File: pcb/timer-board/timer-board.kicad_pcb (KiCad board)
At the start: 2 copper layers, 0 parts

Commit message: Connect OLED display, position main components
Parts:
- added C1: C-100n-0402, DW-footprints:C_0402_1005Metric, B.Cu at (104.8, 123.9)
- added C10: C-2u2-0402, DW-footprints:C_0402_1005Metric, B.Cu at (134.1, 132.8)
- added C11: C-100n-0402, DW-footprints:C_0402_1005Metric, B.Cu at (132.3, 126.1)
- added C12: C-100n-0402, DW-footprints:C_0402_1005Metric, B.Cu at (128.3, 131.3)
- added C13: C-100n-0402, DW-footprints:C_0402_1005Metric, B.Cu at (120.1, 130.6)
- added C14: C-100n-0402, DW-footprints:C_0402_1005Metric, B.Cu at (117.8, 120.3)
- added C15: C-4u7-0402, DW-footprints:C_0402_1005Metric, B.Cu at (133.1, 132.8)
- added C16: C-4u7-0402, DW-footprints:C_0402_1005Metric, B.Cu at (124.8, 132.6)
- added C2: C-4u7-0402, DW-footprints:C_0402_1005Metric, B.Cu at (115.2, 121.9)
- added C3: C-4u7-0402, DW-footprints:C_0402_1005Metric, B.Cu at (111.2, 122.0)
- added C6: C-1u-0402, DW-footprints:C_0402_1005Metric, B.Cu at (117.6, 133.2)
- added C7: C-4u7-0402, DW-footprints:C_0402_1005Metric, B.Cu at (121.8, 131.3)
- added C8: C-1u-0402, DW-footprints:C_0402_1005Metric, B.Cu at (115.6, 133.2)
- added C9: C-100n-0402, DW-footprints:C_0402_1005Metric, B.Cu at (132.8, 119.7)
- added D1: PESD5Z5, DW-footprints:D_SOD-523, B.Cu at (110.0, 134.3)
- added D2: TPD2E2U06DCKR, DW-footprints:SOT-323, B.Cu at (110.7, 131.2)
- added DISP1: N096-2864KSWEG01-H30, DW-footprints:N096-2864KSWEG01-H30, B.Cu at (125.3, 135.2)
- added J1: USB-C_USB-310F-B-SU, DW-footprints:USB-C-Receptacle_USB-310-B-SU, B.Cu at (103.7, 130.0)
- added J11: Programming connector, DW-footprints:Custom-programming-connector-1x6_P1.27mm, B.Cu at (167.4, 125.3)
- added M1: DM-OLED096-636, DW-footprints:DM-OLED096-636, F.Cu at (121.2, 117.5)
- added R1: R-330r-0402, DW-footprints:R_0402_1005Metric, B.Cu at (105.8, 123.9)
- added R2: R-5k1-0402, DW-footprints:R_0402_1005Metric, B.Cu at (110.0, 126.0)
- added R3: R-5k1-0402, DW-footprints:R_0402_1005Metric, B.Cu at (111.1, 126.0)
- added R5: R-5k1-0402, DW-footprints:R_0402_1005Metric, B.Cu at (123.8, 132.6)
- added R6: R-390k-0402, DW-footprints:R_0402_1005Metric, B.Cu at (132.0, 132.8)
- added REF**: NPTH_3.2mm, DW-footprints:NPTH_3.2mm, F.Cu at (103.5, 146.5)
- added REF**: NPTH_3.2mm, DW-footprints:NPTH_3.2mm, F.Cu at (146.5, 113.5)
- added REF**: NPTH_3.2mm, DW-footprints:NPTH_3.2mm, F.Cu at (103.5, 113.5)
- added REF**: NPTH_3.2mm, DW-footprints:NPTH_3.2mm, F.Cu at (146.5, 146.5)
- added SW1: SW_KMR211NGLFS, DW-footprints:SW_KMR211NGLFS, B.Cu at (137.0, 107.0)
- added SW2: SW_KMR211NGLFS, DW-footprints:SW_KMR211NGLFS, F.Cu at (115.0, 144.3)
- added SW3: SW_KMR211NGLFS, DW-footprints:SW_KMR211NGLFS, F.Cu at (135.0, 144.3)
- added SW4: SW_KMR211NGLFS, DW-footprints:SW_KMR211NGLFS, F.Cu at (125.0, 144.3)
- added U1: STM32F411RET6, DW-footprints:LQFP-64_10x10mm_P0.5mm, B.Cu at (125.0, 124.0)
- added U2: TSSP58038, OptoDevice:Vishay_MINICAST-3Pin, B.Cu at (122.5, 113.8)
- added U3: AMS1117-3.3, Package_TO_SOT_SMD:SOT-223-3_TabPin2, B.Cu at (112.5, 116.8)
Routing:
- net GND: track 0.00 -> 17.5 mm, vias 0 -> 11
- net +3V3: track 0.00 -> 15.1 mm, vias 0 -> 6
- net /MCU/OSC_IN: track 0.00 -> 5.39 mm
- net /MCU/OSC_OUT: track 0.00 -> 3.73 mm
- net /Display/C1N: track 0.00 -> 2.09 mm
- net /Display/C2P: track 0.00 -> 2.09 mm
- net /Display/VCC: track 0.00 -> 2.00 mm
- net /Display/IREF: track 0.00 -> 2.00 mm
- net /Display/C1P: track 0.00 -> 2.00 mm
- net /Display/C2N: track 0.00 -> 1.97 mm
- net /Display/VCOMH: track 0.00 -> 1.85 mm
- net Net-(U1-VCAP1): track 0.00 -> 1.50 mm
- net /MCU/USB.D+: track 0.00 -> 0.95 mm
- net /MCU/USB.D-: track 0.00 -> 0.82 mm
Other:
- board outline added: 50 x 40 mm

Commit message: Layout power planes and different signals
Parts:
- removed M1: DM-OLED096-636, DW-footprints:DM-OLED096-636
- added C4: C-100n-0402, DW-footprints:C_0402_1005Metric, B.Cu at (128.8, 116.8)
- added TP1: TP_SMD_1mm, DW-footprints:TP_SMD_1mm, F.Cu at (140.6, 133.4)
- added TP2: TP_SMD_1mm, DW-footprints:TP_SMD_1mm, F.Cu at (142.9, 133.4)
- added kibuzzard-68E6B0E6: G***, kibuzzard-68E6B0E6, B.Cu at (116.2, 118.4)
- added kibuzzard-68E6B138: G***, kibuzzard-68E6B138, B.Cu at (115.5, 117.1)
- added kibuzzard-68E6B152: G***, kibuzzard-68E6B152, B.Cu at (115.5, 115.8)
- added kibuzzard-68E6B17C: G***, kibuzzard-68E6B17C, B.Cu at (116.2, 114.6)
- added kibuzzard-68E6B182: G***, kibuzzard-68E6B182, B.Cu at (116.2, 113.3)
- added kibuzzard-68FD2D82: G***, kibuzzard-68FD2D82, B.Cu at (116.5, 112.0)
- moved J11 50.1 mm to (117.8, 118.4)
- moved U3 23.0 mm to (108.5, 139.4), turned to 0 degrees
- moved C2 19.7 mm to (103.4, 137.6), turned to 90 degrees
- moved C3 19.6 mm to (103.4, 139.9), turned to 90 degrees
- moved SW1 8.70 mm to (134.2, 115.2), turned to -90 degrees
- moved R3 7.33 mm to (110.2, 133.3), turned to 90 degrees
- moved R2 1.83 mm to (109.0, 127.5)
- moved C1 1.58 mm to (106.4, 123.8)
- moved R1 1.58 mm to (107.4, 123.8)
- moved D1 1.41 mm to (109.0, 133.3)
- moved D2 1.10 mm to (109.9, 130.5)
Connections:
- J11 pad 4: /MCU/~{RST} -> /MCU/NRST
- J11 pad 6: /MCU/BOOT0 -> unconnected-(J11-Pad6)
- SW2 pad 3: unconnected-(SW2-Pad3) -> GND
- SW2 pad 4: unconnected-(SW2-Pad4) -> GND
- SW3 pad 3: unconnected-(SW3-Pad3) -> GND
- SW3 pad 4: unconnected-(SW3-Pad4) -> GND
- SW4 pad 3: unconnected-(SW4-Pad3) -> GND
- SW4 pad 4: unconnected-(SW4-Pad4) -> GND
- U1 pad 40: unconnected-(U1-PC9-Pad40) -> /Display/I2C.SDA
- U1 pad 41: unconnected-(U1-PA8-Pad41) -> /Display/I2C.SCL
- U2 pad 1: unconnected-(U2-OUT-Pad1) -> /IR receiver/GATE_TRIGGER
- U2 pad 2: unconnected-(U2-GND-Pad2) -> GND
- U2 pad 3: unconnected-(U2-Vs-Pad3) -> +3V3
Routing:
- net GND: track 17.5 -> 50.4 mm, vias 11 -> 41
- net /Display/I2C.SCL: track 0.00 -> 25.7 mm
- net /Display/I2C.SDA: track 0.00 -> 20.5 mm
- net /MCU/NRST: track 0.00 -> 20.5 mm
- net /MCU/USB.D-: track 0.82 -> 18.5 mm
- net /MCU/USB.D+: track 0.95 -> 17.3 mm
- net /MCU/BOOT0: track 0.00 -> 14.1 mm
- net /MCU/SWDIO: track 0.00 -> 6.90 mm
- net /MCU/SWCLK: track 0.00 -> 4.91 mm
- net /Power/VBUS: track 0.00 -> 3.65 mm
- net Net-(J1-CC1): track 0.00 -> 3.46 mm
- net Net-(J1-SHIELD): track 0.00 -> 3.19 mm
- net Net-(J1-CC2): track 0.00 -> 1.75 mm
- added copper zone on B.Cu, net +3V3
- added copper zone on F.Cu, net GND

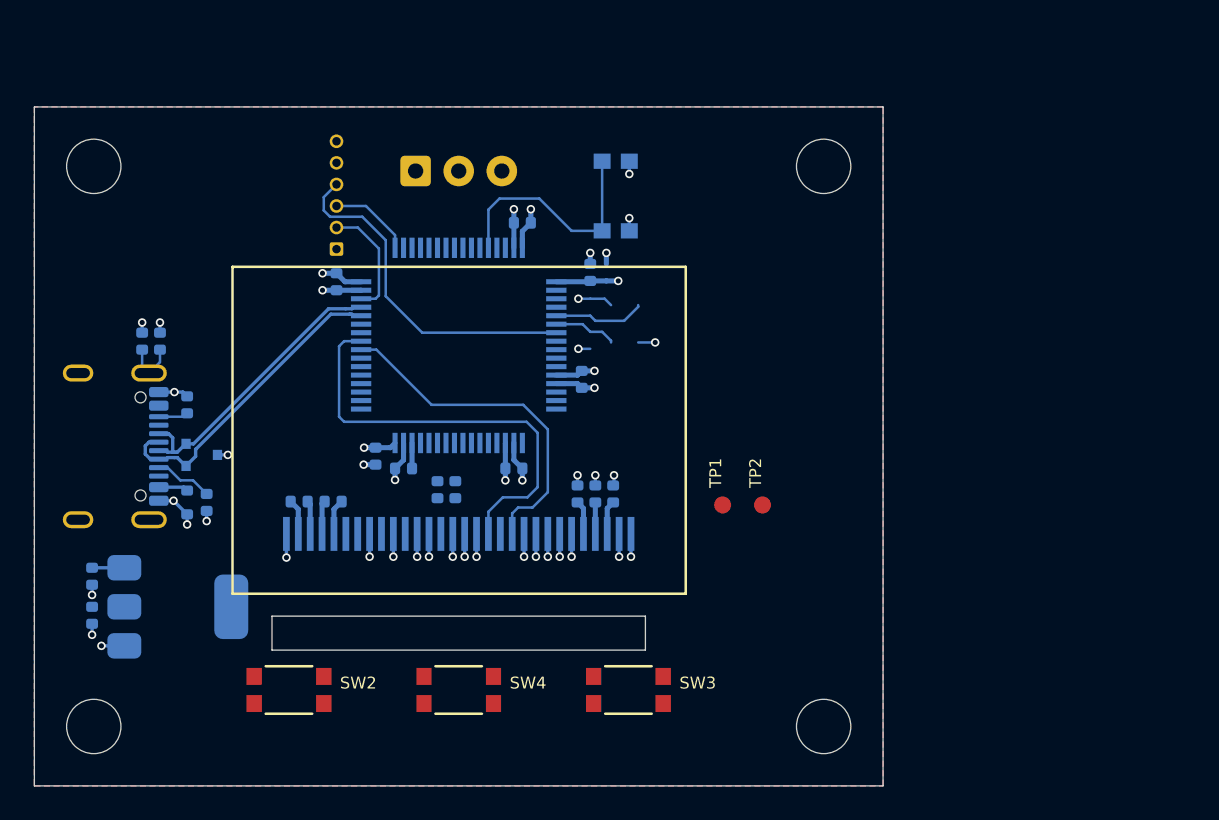
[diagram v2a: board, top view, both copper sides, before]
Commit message: Finish uncompleted schematic sections, layout most of the PCB
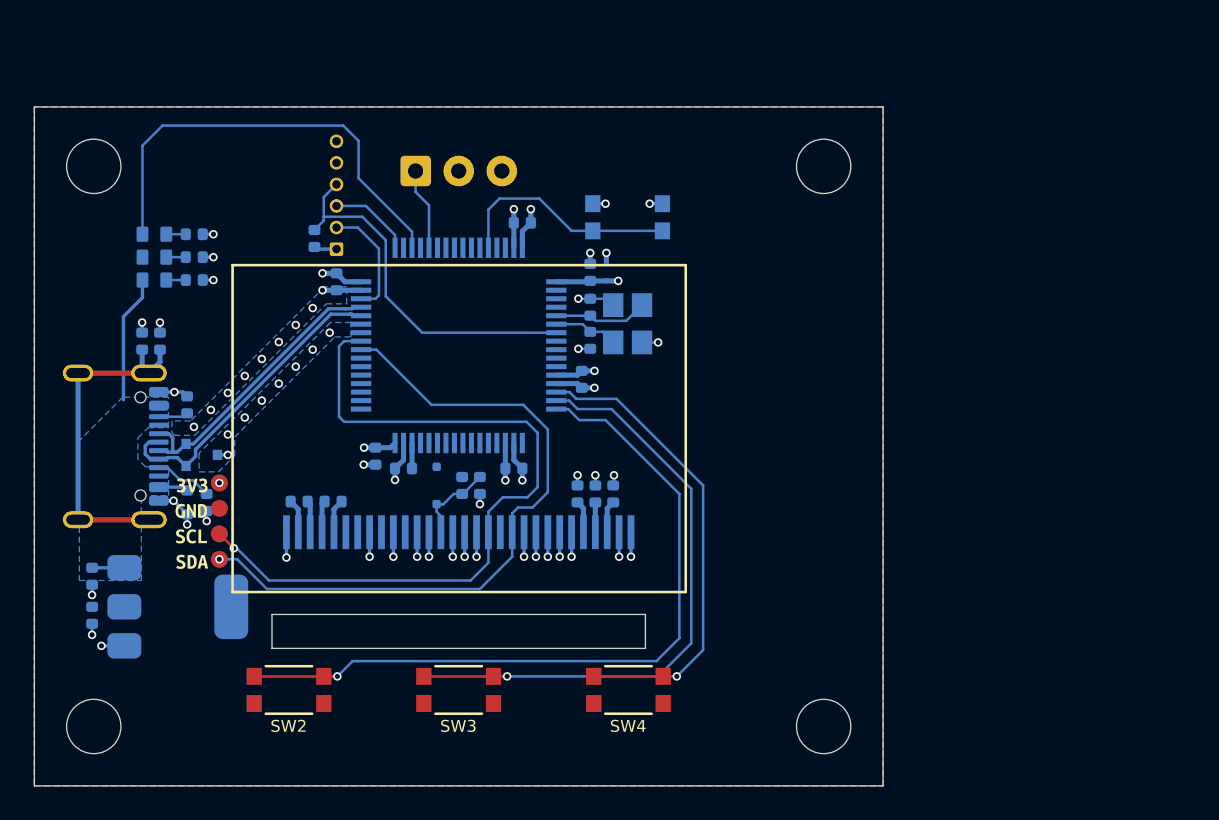
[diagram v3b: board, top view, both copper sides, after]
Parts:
- added C18: C-33p-0402, DW-footprints:C_0402_1005Metric, B.Cu at (132.8, 123.8)
- added C5: C-33p-0402, DW-footprints:C_0402_1005Metric, B.Cu at (132.8, 121.8)
- added D3: LED-R-0603_KT-0603R, DW-footprints:LED_0603_1608Metric_R, B.Cu at (107.1, 117.5)
- added D4: LED-R-0603_KT-0603R, DW-footprints:LED_0603_1608Metric_R, B.Cu at (107.1, 120.2)
- added D5: LED-R-0603_KT-0603R, DW-footprints:LED_0603_1608Metric_R, B.Cu at (107.1, 118.8)
- added D6: 1N4148WS-AU, DW-footprints:D_SOD-323F, B.Cu at (123.7, 132.3)
- added R4: R-1k-0402, DW-footprints:R_0402_1005Metric, B.Cu at (109.4, 120.2)
- added R7: R-1k-0402, DW-footprints:R_0402_1005Metric, B.Cu at (109.4, 118.8)
- added R8: R-1k-0402, DW-footprints:R_0402_1005Metric, B.Cu at (109.4, 117.5)
- added R9: R-5k1-0402, DW-footprints:R_0402_1005Metric, B.Cu at (116.5, 117.8)
- added TP3: TP_SMD_1mm, DW-footprints:TP_SMD_1mm, F.Cu at (110.9, 132.2)
- added TP4: TP_SMD_1mm, DW-footprints:TP_SMD_1mm, F.Cu at (110.9, 133.7)
- added Y1: X322512MSB4SI, DW-footprints:Crystal_SMD_3225-4Pin_3.2x2.5mm, B.Cu at (134.9, 122.8)
- added kibuzzard-690B1D8E: G***, kibuzzard-690B1D8E, F.Cu at (109.3, 136.8)
- added kibuzzard-690B1DCB: G***, kibuzzard-690B1DCB, F.Cu at (109.2, 135.3)
- added kibuzzard-690B1DD3: G***, kibuzzard-690B1DD3, F.Cu at (109.3, 132.3)
- added kibuzzard-690B1DD8: G***, kibuzzard-690B1DD8, F.Cu at (109.2, 133.8)
- added kibuzzard-690B8D6F: G***, kibuzzard-690B8D6F, B.Cu at (134.9, 114.3)
- moved TP2 32.2 mm to (110.9, 136.7), turned to 180 degrees
- moved TP1 29.7 mm to (110.9, 135.2), turned to 180 degrees
- moved C16 1.47 mm to (126.2, 132.3), turned to 90 degrees
- moved R5 1.47 mm to (125.2, 132.3)
- moved SW1 1.43 mm to (134.9, 116.5), turned to 0 degrees
- moved DISP1 0.10 mm to (125.3, 135.1)
- renumbered SW4 to SW3, SW3 to SW4
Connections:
- net Net-(DISP1-~{RES}) renamed /Display/~{RES}
- SW2 pad 1: unconnected-(SW2-Pad1) -> /MCU/BTN1
- SW2 pad 2: unconnected-(SW2-Pad2) -> /MCU/BTN1
- SW3 pad 1: unconnected-(SW4-Pad1) -> /MCU/BTN2
- SW3 pad 2: unconnected-(SW4-Pad2) -> /MCU/BTN2
- SW4 pad 1: unconnected-(SW3-Pad1) -> /MCU/BTN3
- SW4 pad 2: unconnected-(SW3-Pad2) -> /MCU/BTN3
- U1 pad 14: unconnected-(U1-PA0-Pad14) -> /MCU/BTN3
- U1 pad 15: unconnected-(U1-PA1-Pad15) -> /MCU/BTN2
- U1 pad 16: unconnected-(U1-PA2-Pad16) -> /MCU/BTN1
- U1 pad 51: unconnected-(U1-PC10-Pad51) -> /MCU/USER_LED
- U1 pad 53: unconnected-(U1-PC12-Pad53) -> /IR receiver/GATE_TRIGGER
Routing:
- net /MCU/BTN1: track 0.00 -> 43.8 mm, vias 0 -> 1
- net /MCU/BTN2: track 0.00 -> 35.8 mm, vias 0 -> 1
- net /MCU/BTN3: track 0.00 -> 27.7 mm, vias 0 -> 1
- net /MCU/USER_LED: track 0.00 -> 26.4 mm
- net /Display/I2C.SDA: track 20.5 -> 40.6 mm, vias 0 -> 1
- net /Display/I2C.SCL: track 25.7 -> 44.8 mm, vias 0 -> 1
- net Net-(J1-SHIELD): track 3.19 -> 20.2 mm
- net /Power/VBUS: track 3.65 -> 11.2 mm
- net /Display/~{RES}: track 0.00 -> 5.06 mm
- net /IR receiver/GATE_TRIGGER: track 0.00 -> 4.85 mm
- net GND: track 50.4 -> 53.0 mm, vias 41 -> 60
- net +3V3: track 15.1 -> 16.5 mm, vias 6 -> 7
- net /MCU/NRST: track 20.5 -> 21.7 mm
- net Net-(D5-C): track 0.00 -> 1.15 mm
- net Net-(D4-C): track 0.00 -> 1.15 mm
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- added copper zone on B.Cu, net /Power/VBUS
- added copper zone on B.Cu, net GND
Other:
- outline, holes or cut-outs redrawn

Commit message: Add 3.5mm jack, fix BOOT0 connection
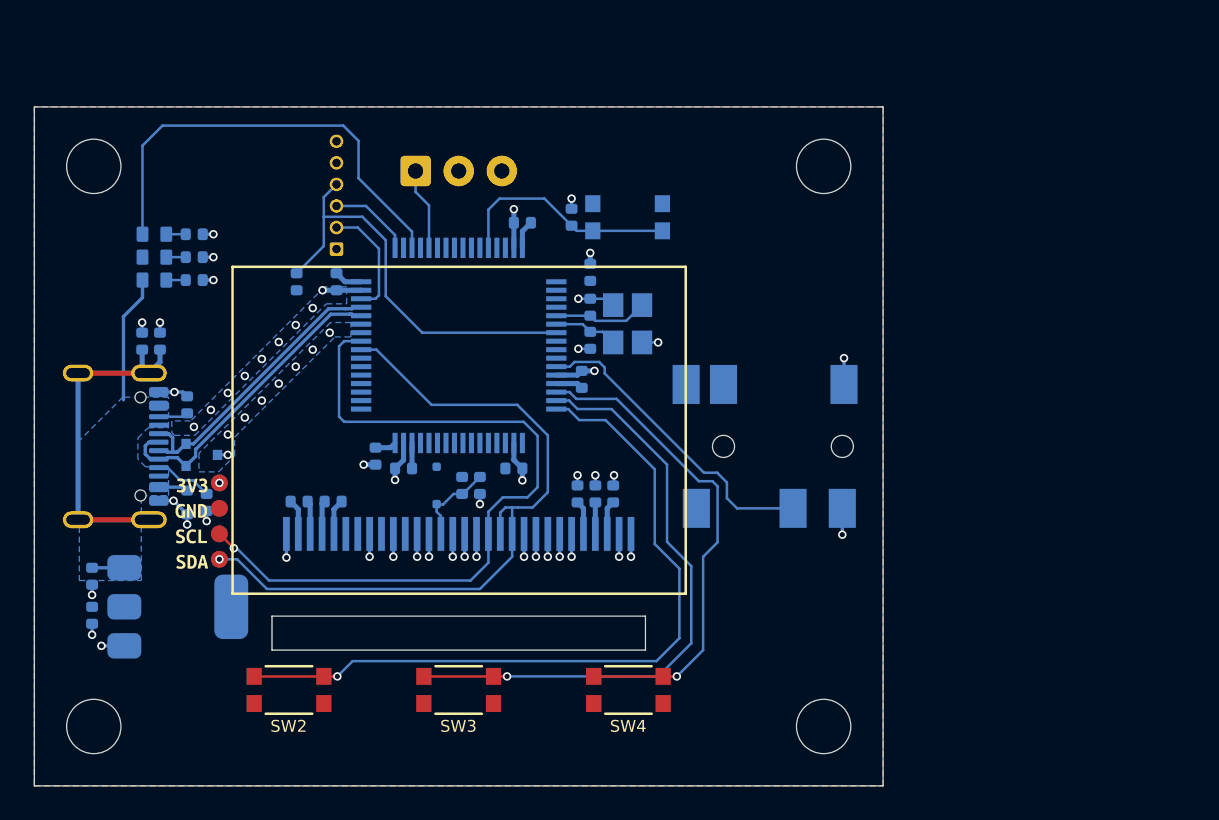
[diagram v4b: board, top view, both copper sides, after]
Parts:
- added J2: Jack_PJ-342, DW-footprints:Jack_PJ-342, B.Cu at (143.1, 130.0)
- added R10: R-5k1-0402, DW-footprints:R_0402_1005Metric, B.Cu at (131.7, 116.5)
- moved R9 2.76 mm to (115.5, 120.3)
- moved DISP1 0.10 mm to (125.3, 135.2)
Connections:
- net /IR receiver/GATE_TRIGGER renamed /IR receiver/GATE_TRIGGER_1
- SW1 pad 3: GND -> +3V3
- SW1 pad 4: GND -> +3V3
- U1 pad 11: unconnected-(U1-PC3-Pad11) -> /IR receiver/GATE_TRIGGER_2
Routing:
- net /IR receiver/GATE_TRIGGER_2: track 0.00 -> 18.4 mm
- net +3V3: track 16.5 -> 6.28 mm, vias 7 -> 1
- net /MCU/NRST: track 21.7 -> 24.7 mm
- net /Display/I2C.SDA: track 40.6 -> 42.7 mm
- net GND: track 53.0 -> 54.5 mm
- net /MCU/BTN3: track 27.7 -> 28.9 mm
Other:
- outline, holes or cut-outs redrawn

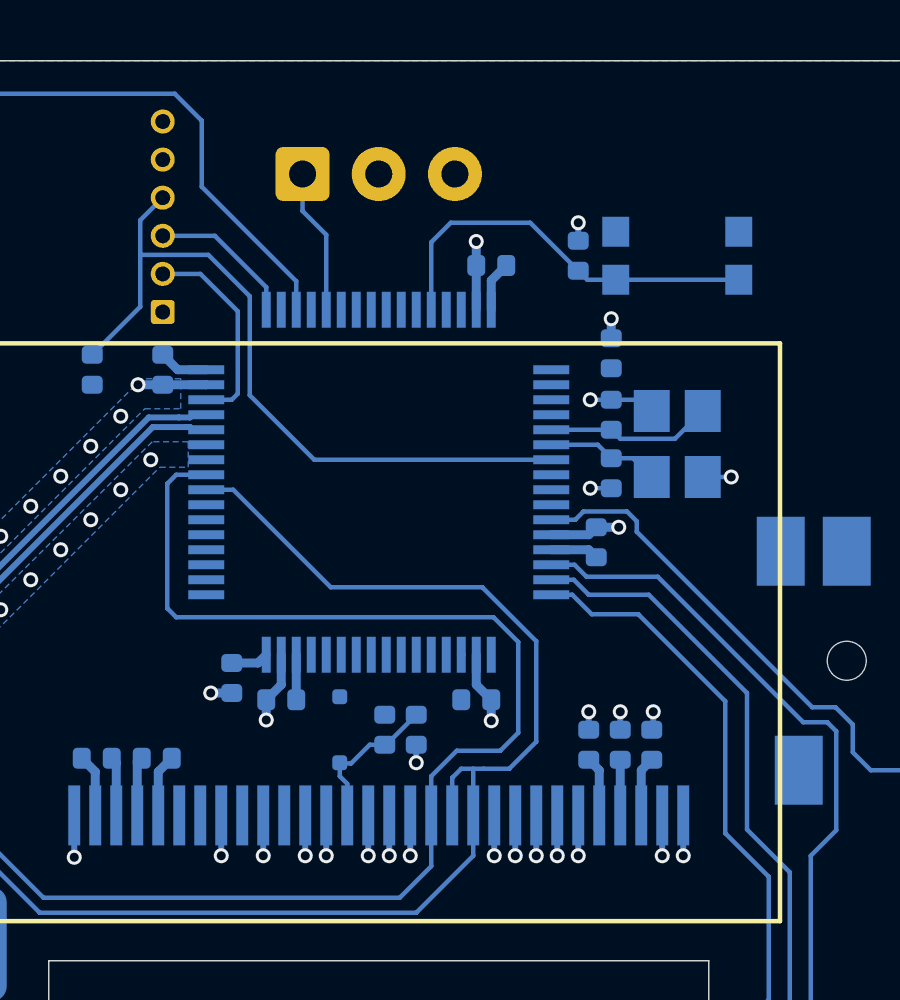
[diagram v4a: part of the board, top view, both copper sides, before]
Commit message: Add I2C pull-up, IR receiver decoupling, LED labels, clear ERC and DRC
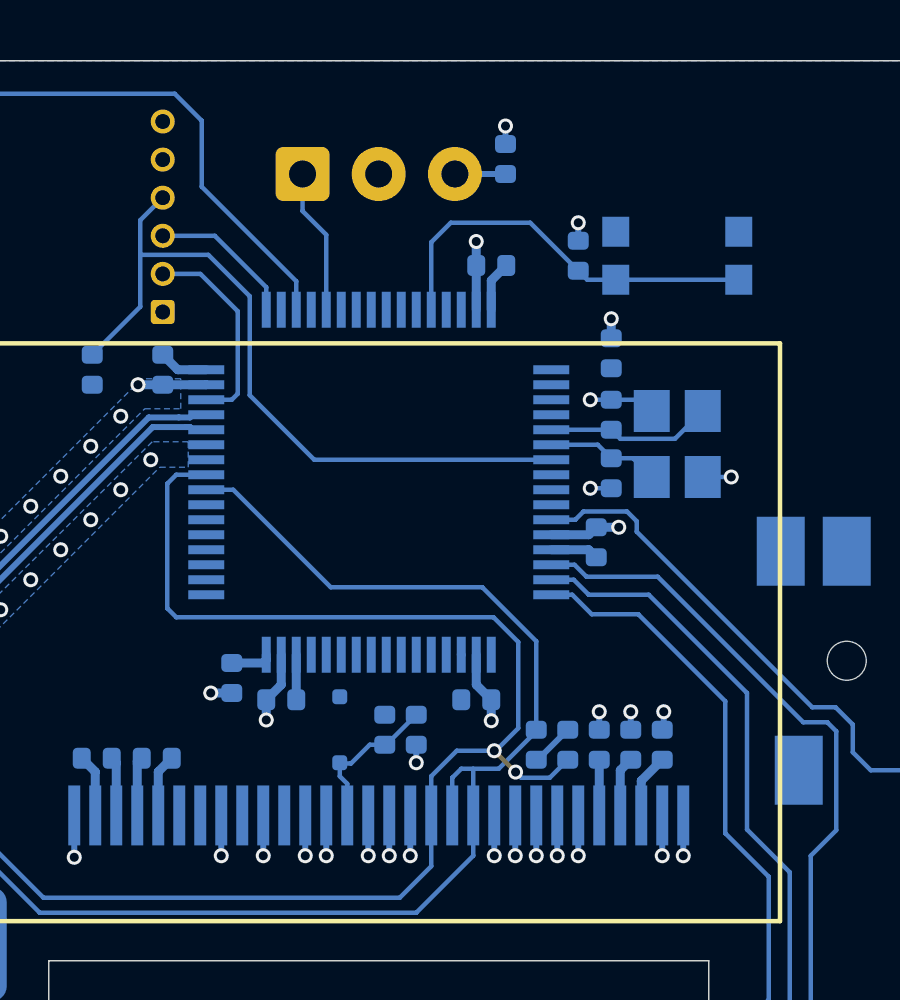
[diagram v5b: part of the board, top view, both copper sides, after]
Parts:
- added C17: C-1u-0402, DW-footprints:C_0402_1005Metric, B.Cu at (129.2, 113.3)
- added R11: R-5k1-0402, DW-footprints:R_0402_1005Metric, B.Cu at (130.2, 132.8)
- added R12: R-5k1-0402, DW-footprints:R_0402_1005Metric, B.Cu at (131.3, 132.8)
- added kibuzzard-691094F6: G***, kibuzzard-691094F6, B.Cu at (104.2, 120.2)
- added kibuzzard-69109507: G***, kibuzzard-69109507, B.Cu at (104.2, 117.5)
- added kibuzzard-69109536: G***, kibuzzard-69109536, B.Cu at (104.2, 118.8)
- moved C10 0.35 mm to (134.4, 132.8)
- moved C15 0.35 mm to (133.4, 132.8)
- moved R6 0.35 mm to (132.3, 132.8)
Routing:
- net +3V3: track 6.28 -> 9.53 mm
- net /Display/I2C.SCL: track 44.7 -> 47.7 mm, vias 1 -> 3
- net GND: track 54.5 -> 55.1 mm, vias 60 -> 61
